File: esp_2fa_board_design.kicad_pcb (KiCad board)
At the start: 2 copper layers, 82 x 45 mm, 53 parts, among them IC1 TPS22919DCKR, J1 Conn_01x02_Female, J2 TYPE-C-31-M-17, J3 Conn_01x02_Female, Q1 DMP2305U-7, SW1 SW_Push, SW2 SW_Push, SW3 BOOT, SW4 RESET, SW5 POWER SWITCH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

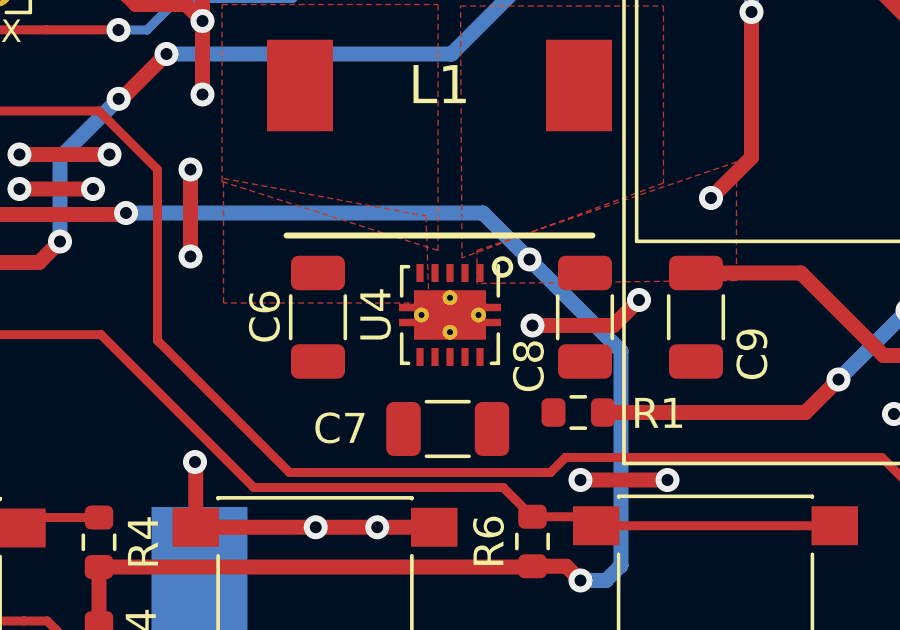
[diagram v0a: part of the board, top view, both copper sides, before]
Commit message: Bridged the splits under the voltage regulator
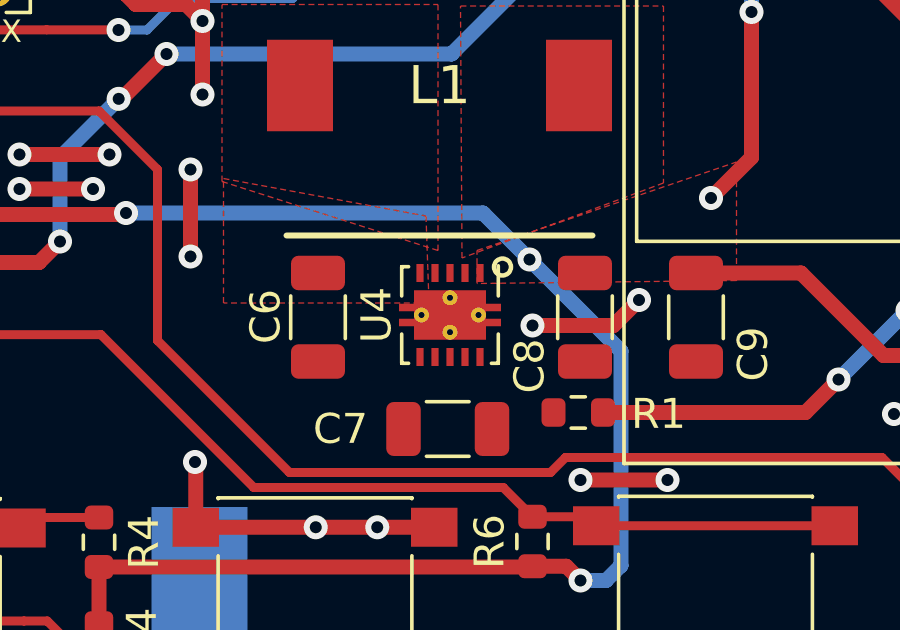
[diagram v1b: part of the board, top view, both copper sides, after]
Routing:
- net GND: track 231.4 -> 234.5 mm
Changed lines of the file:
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@@
     (thickness 1.6)
     (drawings 25)
-    (tracks 564)
+    (tracks 566)
     (zones 0)
     (modules 53)
@@
   (via (at 135.85 109) (size 0.8) (drill 0.4) (layers F.Cu B.Cu) (net 3))
   (segment (start 138.75 109) (end 135.85 109) (width 0.5) (layer F.Cu) (net 3))
+  (segment (start 131.5 102.925) (end 131.5 104.075) (width 0.5) (layer B.Cu) (net 3))
+  (segment (start 130.55 103.5) (end 132.45 103.5) (width 0.5) (layer B.Cu) (net 3))
   (segment (start 102.3 109.875) (end 102.275 109.85) (width 0.5) (layer F.Cu) (net 4))
   (segment (start 105.55 109.2) (end 105.55 109.25) (width 0.5) (layer F.Cu) (net 4))

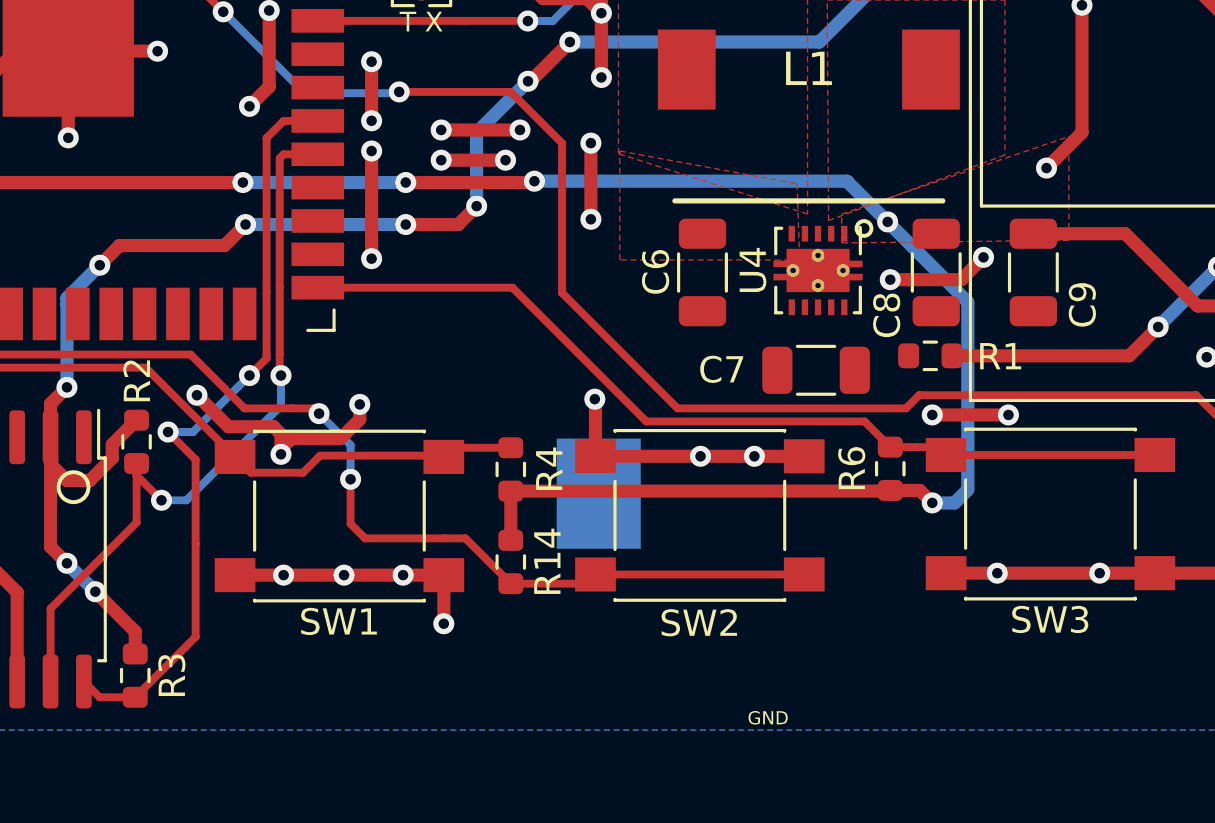
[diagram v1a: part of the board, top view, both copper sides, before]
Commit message: Minor fixes - Removed routes with 90 degree turns
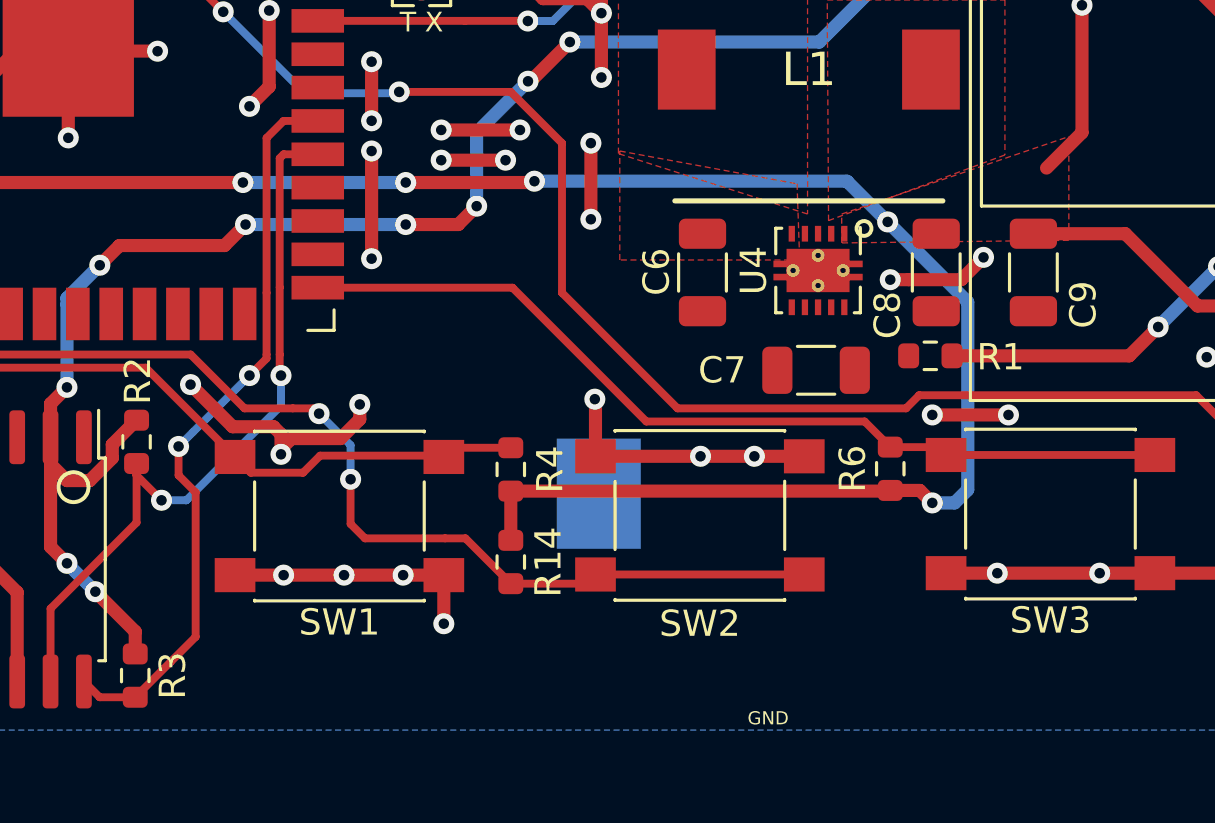
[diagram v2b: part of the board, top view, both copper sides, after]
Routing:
- net /IO18_SCL: track 29.2 -> 28.3 mm
- net +3V3: vias 10 -> 9
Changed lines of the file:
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@@
     (thickness 1.6)
     (drawings 25)
-    (tracks 566)
+    (tracks 564)
     (zones 0)
     (modules 53)
@@
   (segment (start 115.7 115.1) (end 117.25 115.1) (width 0.5) (layer F.Cu) (net 3))
   (via (at 115.7 115.1) (size 0.8) (drill 0.4) (layers F.Cu B.Cu) (net 3))
-  (via (at 107.85 108.25) (size 0.8) (drill 0.4) (layers F.Cu B.Cu) (net 3))
   (segment (start 96.5 113.2) (end 96.5 113.139998) (width 0.3) (layer F.Cu) (net 3))
   (via (at 93.2 114.95) (size 0.8) (drill 0.4) (layers F.Cu B.Cu) (net 3))
@@
   (segment (start 111.05 109.734315) (end 110.765685 109.45) (width 0.5) (layer F.Cu) (net 3))
   (segment (start 111.05 110.3) (end 111.05 109.734315) (width 0.5) (layer F.Cu) (net 3))
-  (segment (start 109.05 109.45) (end 107.85 108.25) (width 0.5) (layer F.Cu) (net 3))
-  (segment (start 110.765685 109.45) (end 109.05 109.45) (width 0.5) (layer F.Cu) (net 3))
   (via (at 134.35 83.25) (size 0.8) (drill 0.4) (layers F.Cu B.Cu) (net 3))
   (segment (start 133.3 84.3) (end 134.35 83.25) (width 0.3) (layer F.Cu) (net 3))
@@
   (segment (start 131.5 102.925) (end 131.5 104.075) (width 0.5) (layer B.Cu) (net 3))
   (segment (start 130.55 103.5) (end 132.45 103.5) (width 0.5) (layer B.Cu) (net 3))
+  (via (at 107.605331 107.844669) (size 0.8) (drill 0.4) (layers F.Cu B.Cu) (net 3))
+  (segment (start 109.210662 109.45) (end 110.765685 109.45) (width 0.5) (layer F.Cu) (net 3))
+  (segment (start 107.605331 107.844669) (end 109.210662 109.45) (width 0.5) (layer F.Cu) (net 3))
   (segment (start 102.3 109.875) (end 102.275 109.85) (width 0.5) (layer F.Cu) (net 4))
   (segment (start 105.55 109.2) (end 105.55 109.25) (width 0.5) (layer F.Cu) (net 4))
@@
   (segment (start 137.2 111.85) (end 137.2 104.7) (width 0.5) (layer B.Cu) (net 8))
   (via (at 141.55 93.40001) (size 0.8) (drill 0.4) (layers F.Cu B.Cu) (net 8))
-  (via (at 140.2 99.6) (size 0.8) (drill 0.4) (layers F.Cu B.Cu) (net 8))
   (segment (start 141.55 98.25) (end 140.2 99.6) (width 0.5) (layer F.Cu) (net 8))
   (segment (start 141.55 93.40001) (end 141.55 98.25) (width 0.5) (layer F.Cu) (net 8))
@@
   (segment (start 110.5 104.35) (end 110.5 106.7) (width 0.3) (layer F.Cu) (net 23))
   (segment (start 110.5 106.7) (end 110.5 106.85) (width 0.3) (layer F.Cu) (net 23))
-  (segment (start 106.85 118.4) (end 105.5 119.75) (width 0.3) (layer F.Cu) (net 23))
   (via (at 109.85 107.5) (size 0.8) (drill 0.4) (layers F.Cu B.Cu) (net 23))
   (segment (start 110.5 106.85) (end 109.85 107.5) (width 0.3) (layer F.Cu) (net 23))
-  (segment (start 106.85 118.4) (end 107.8 117.45) (width 0.3) (layer F.Cu) (net 23))
-  (segment (start 107.8 117.45) (end 107.8 113.9) (width 0.3) (layer F.Cu) (net 23))
-  (segment (start 107.8 110.7) (end 107.45 110.35) (width 0.3) (layer F.Cu) (net 23))
-  (segment (start 107.8 113.9) (end 107.8 110.7) (width 0.3) (layer F.Cu) (net 23))
-  (via (at 106.75 109.65) (size 0.8) (drill 0.4) (layers F.Cu B.Cu) (net 23))
-  (segment (start 107.45 110.35) (end 106.75 109.65) (width 0.3) (layer F.Cu) (net 23))
   (segment (start 107.7 109.65) (end 109.85 107.5) (width 0.3) (layer B.Cu) (net 23))
-  (segment (start 106.75 109.65) (end 107.7 109.65) (width 0.3) (layer B.Cu) (net 23))
+  (via (at 107.15 110.2) (size 0.8) (drill 0.4) (layers F.Cu B.Cu) (net 23))
+  (segment (start 107.7 109.65) (end 107.15 110.2) (width 0.3) (layer B.Cu) (net 23))
+  (segment (start 106.85 118.4) (end 105.5 119.75) (width 0.3) (layer F.Cu) (net 23))
+  (segment (start 107.8 117.45) (end 106.85 118.4) (width 0.3) (layer F.Cu) (net 23))
+  (segment (start 107.8 111.95) (end 107.8 117.45) (width 0.3) (layer F.Cu) (net 23))
+  (segment (start 107.15 111.3) (end 107.8 111.95) (width 0.3) (layer F.Cu) (net 23))
+  (segment (start 107.15 110.2) (end 107.15 111.3) (width 0.3) (layer F.Cu) (net 23))
   (segment (start 117.6 110.25) (end 117.25 110.6) (width 0.3) (layer F.Cu) (net 24))
   (segment (start 119.8 110.25) (end 117.6 110.25) (width 0.3) (layer F.Cu) (net 24))

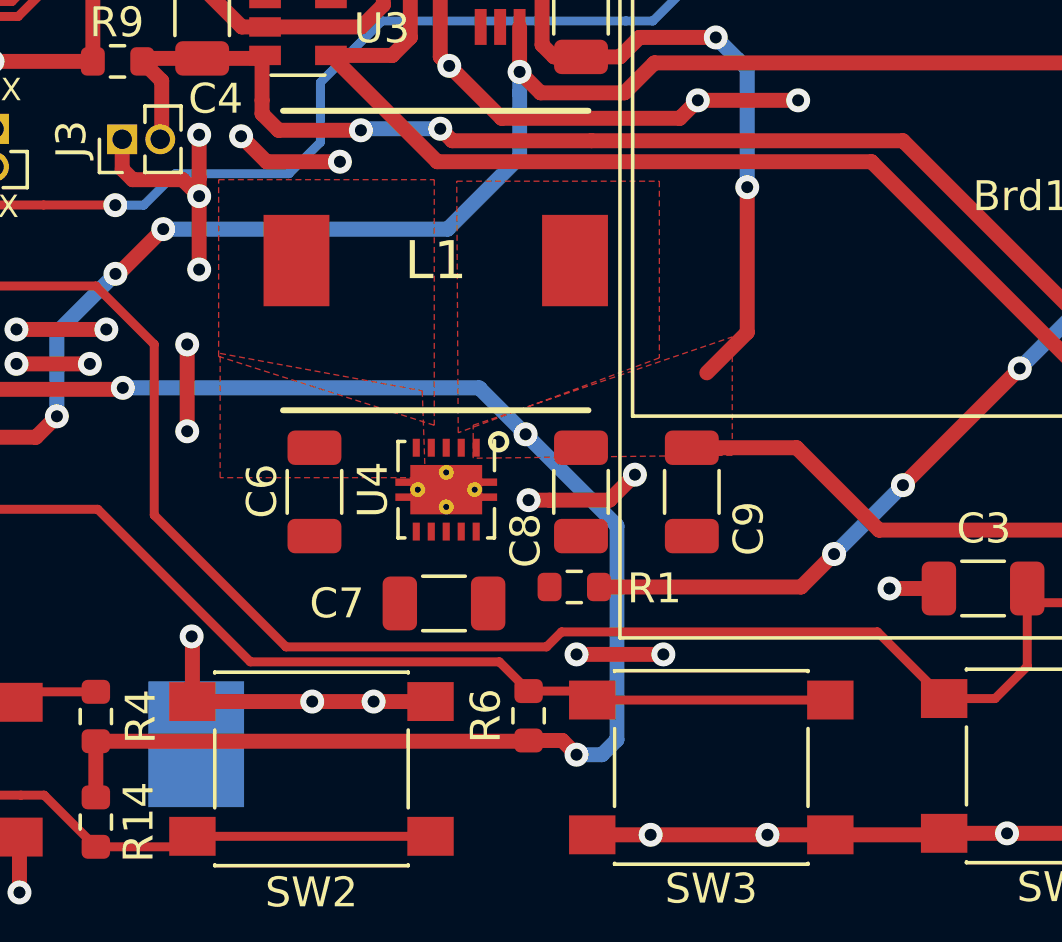
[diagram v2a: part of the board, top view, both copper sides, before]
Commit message: Completed pcb routing, minor touch ups and placing testpoints remaining
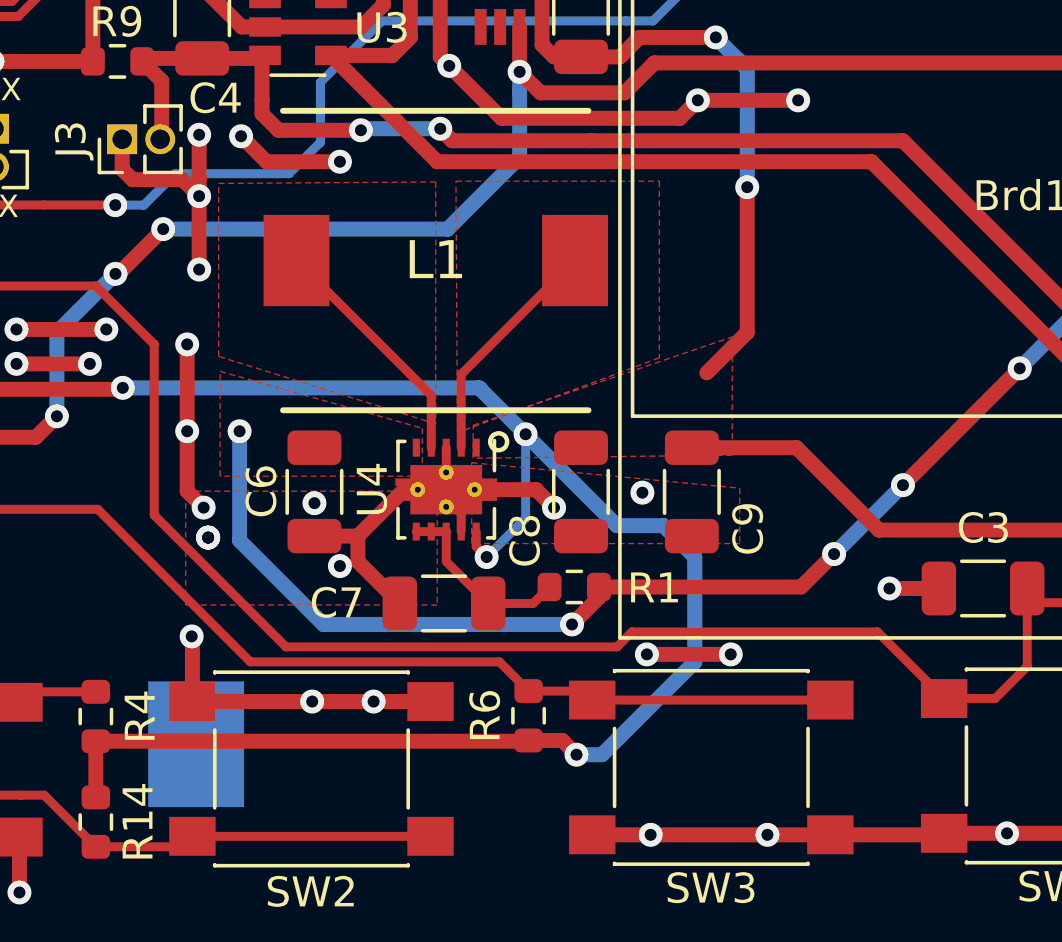
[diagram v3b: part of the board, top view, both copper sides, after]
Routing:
- net Net-(C6-Pad1): track 37.8 -> 55.3 mm, vias 4 -> 6
- net GND: track 234.9 -> 245.5 mm, vias 66 -> 71
- net +3V3: track 127.1 -> 135.8 mm, vias 9 -> 10
- net Net-(L1-Pad1): track 0.00 -> 8.11 mm
- net Net-(L1-Pad2): track 0.00 -> 7.82 mm
- net Net-(C7-Pad1): track 0.00 -> 6.26 mm
- added copper zone on F.Cu, net GND
- added copper zone on F.Cu, net Net-(C6-Pad1)
- removed copper zone on F.Cu, net /V_INPUT

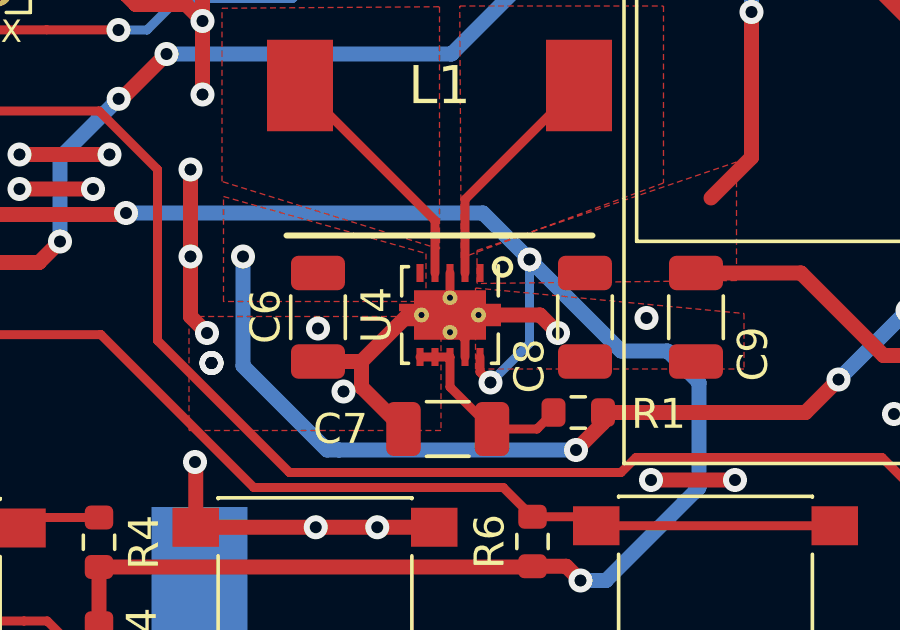
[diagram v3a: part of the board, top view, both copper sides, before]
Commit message: Removed thermal relief from ground plane as not using any tht components
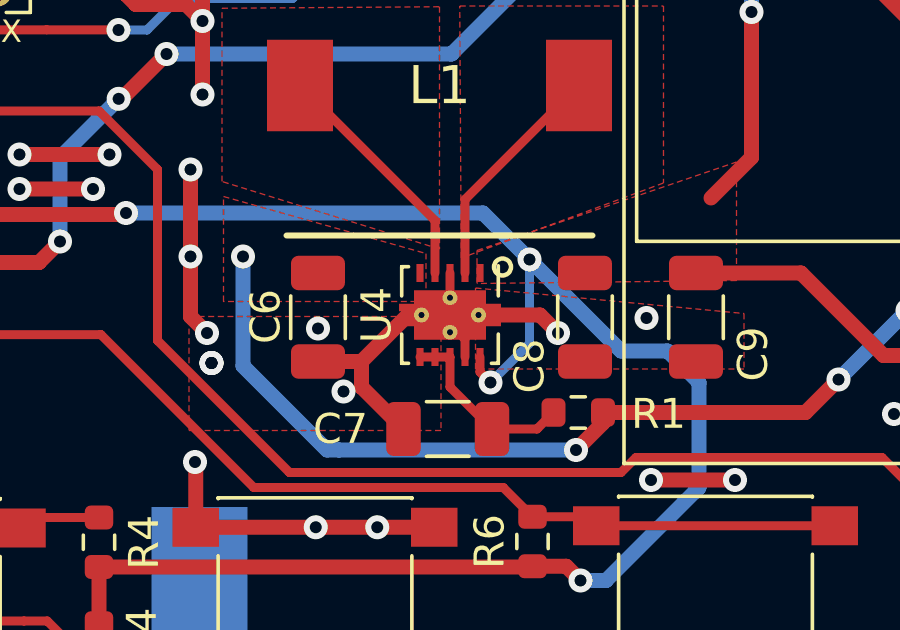
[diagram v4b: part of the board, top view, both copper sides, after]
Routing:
- net GND: track 245.5 -> 242.5 mm
